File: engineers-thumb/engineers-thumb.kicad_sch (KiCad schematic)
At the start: 46 parts, among them J1 power, J2 Conn_01x06_Female, Q1 BC556, U1 LM13700, U2 TL074

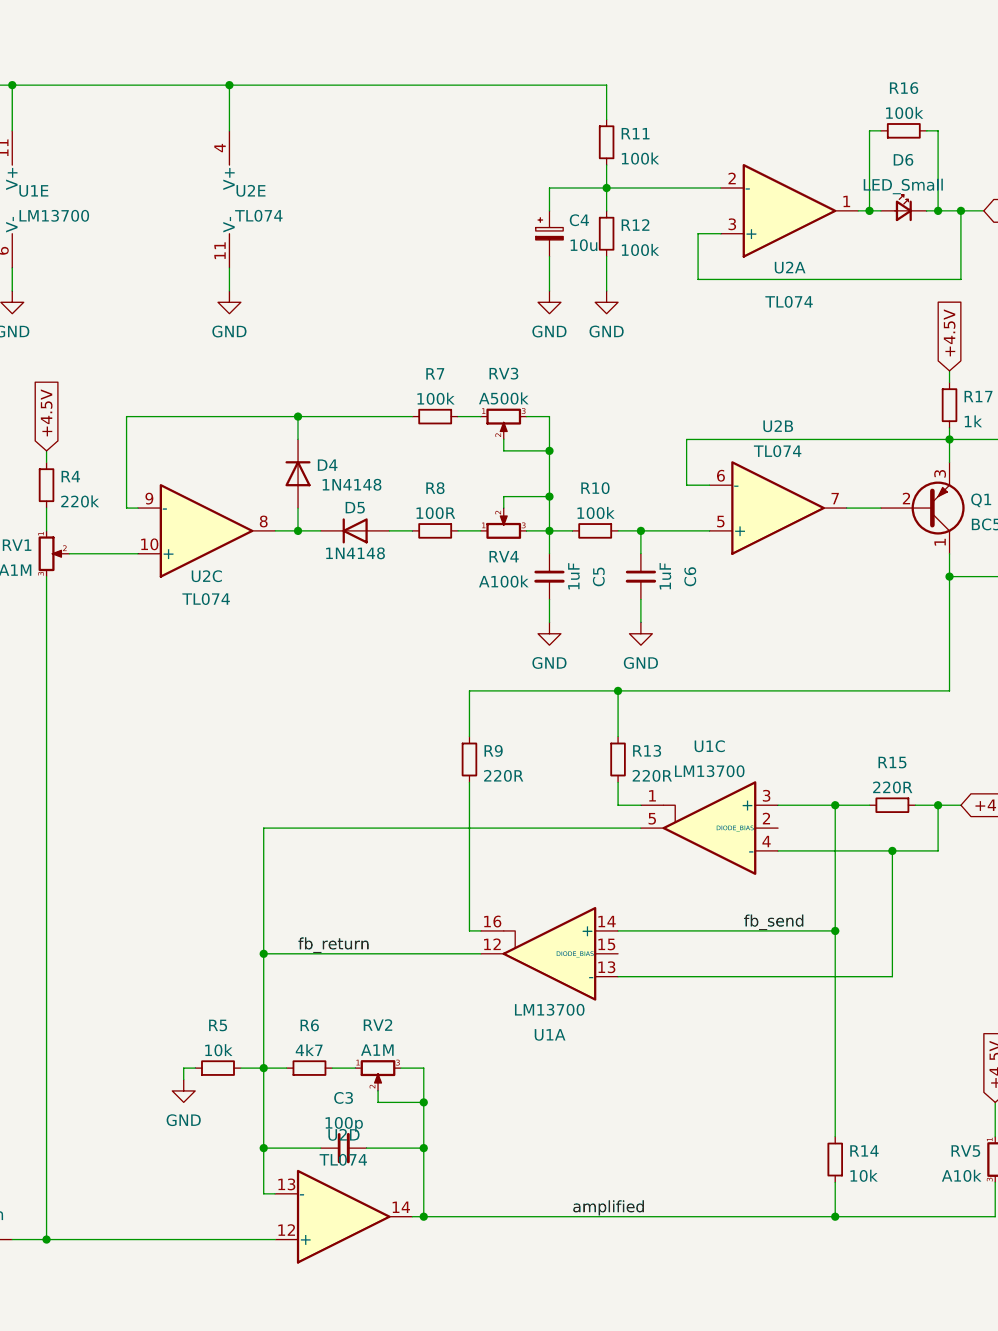
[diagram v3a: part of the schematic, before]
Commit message: Added compressor and psu schematics.
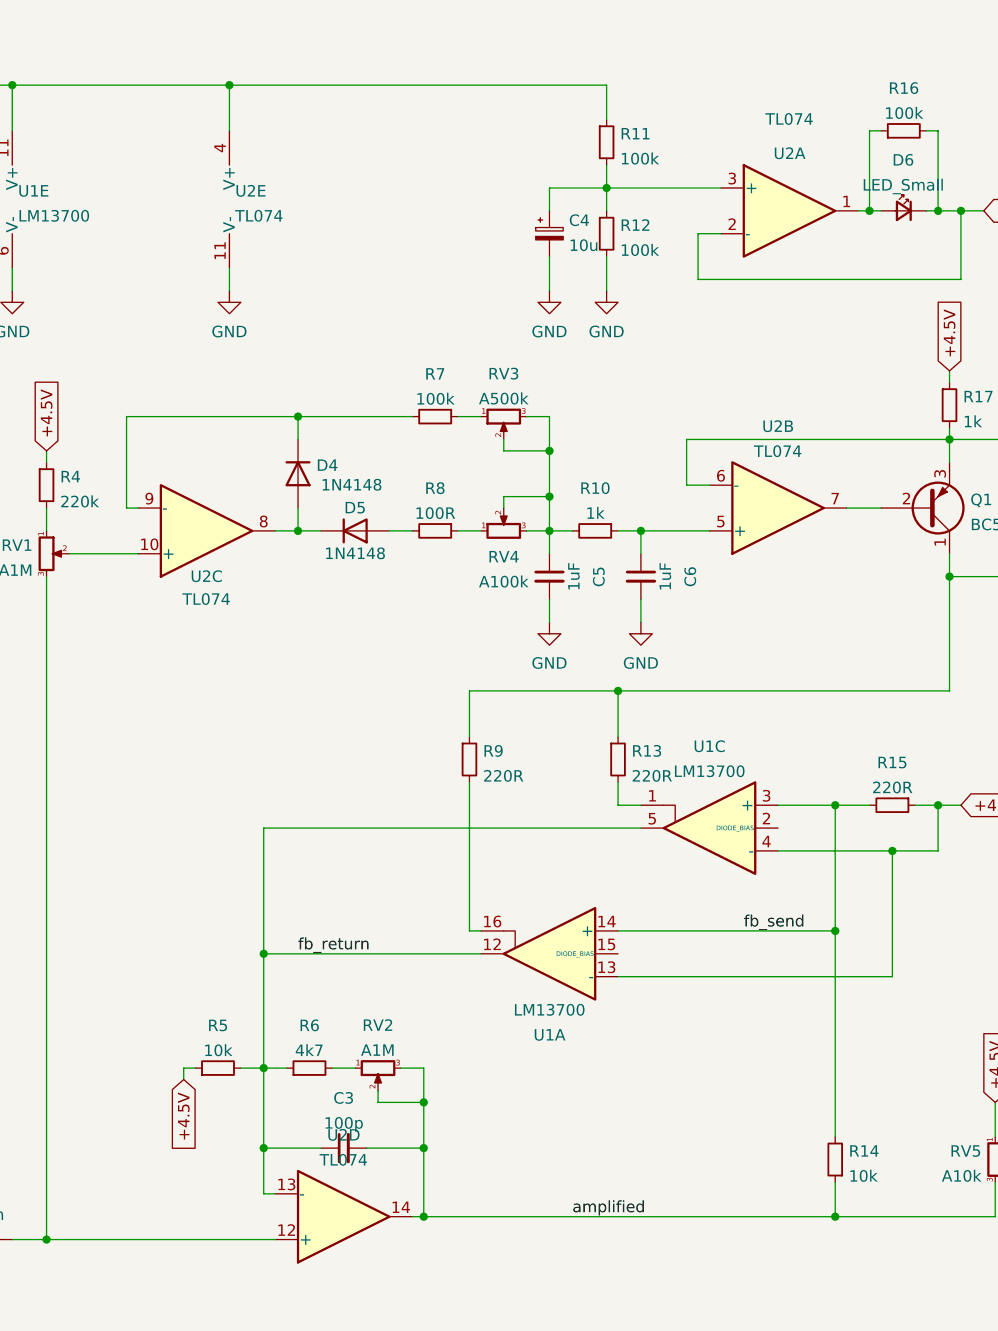
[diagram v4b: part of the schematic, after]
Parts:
- R10: value 100k -> 1k
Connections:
- net +4.5V: now also R5.1, U2.2 (-); no longer U2.3 (+)
- net GND: no longer R5.1
- net at C4.1, R11.2, R12.1: now also U2.3 (+); no longer U2.2 (-)
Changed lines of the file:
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@@
+    )
+  )
+  (global_label "+4.5V" (shape input) (at 88.9 130.81 270) (fields_autoplaced)
+    (effects (font (size 1.27 1.27)) (justify right))
+    (property "Intersheet References" "${INTERSHEET_REFS}" (id 0) (at 88.9794 138.9079 90)
+      (effects (font (size 1.27 1.27)) (justify right) hide)
     )
   )
@@
     (in_bom yes) (on_board yes) (fields_autoplaced)
     (property "Reference" "R10" (id 0) (at 134.62 65.1469 90))
-    (property "Value" "100k" (id 1) (at 134.62 67.922 90))
+    (property "Value" "1k" (id 1) (at 134.62 67.922 90))
     (property "Footprint" "PartsStash:R_Axial_DIN0207_L6.3mm_D2.5mm_P7.62mm_Horizontal" (id 2) (at 134.62 69.85 0)
       (effects (font (size 1.27 1.27)) hide)
@@
     (pin "11")
     (pin "6")
-  )
-  (symbol (lib_id "power:GND") (at 88.9 130.81 0) (unit 1)
-    (in_bom yes) (on_board yes) (fields_autoplaced)
-    (property "Reference" "#PWR08" (id 0) (at 88.9 137.16 0)
-      (effects (font (size 1.27 1.27)) hide)
-    )
-    (property "Value" "GND" (id 1) (at 88.9 135.3725 0))
-    (property "Footprint" "" (id 2) (at 88.9 130.81 0)
-      (effects (font (size 1.27 1.27)) hide)
-    )
-    (property "Datasheet" "" (id 3) (at 88.9 130.81 0)
-      (effects (font (size 1.27 1.27)) hide)
-    )
-    (pin "1")
   )
   (symbol (lib_id "power:GND") (at 218.44 151.13 0) (unit 1)
@@
     (pin "3")
   )
-  (symbol (lib_id "Amplifier_Operational:TL074") (at 156.21 34.29 0) (mirror x) (unit 1)
+  (symbol (lib_id "Amplifier_Operational:TL074") (at 156.21 34.29 0) (unit 1)
     (in_bom yes) (on_board yes)
-    (property "Reference" "U2" (id 0) (at 156.21 40.64 0))
-    (property "Value" "TL074" (id 1) (at 156.21 44.45 0))
-    (property "Footprint" "Package_DIP:DIP-14_W7.62mm_Socket_LongPads" (id 2) (at 154.94 36.83 0)
-      (effects (font (size 1.27 1.27)) hide)
-    )
-    (property "Datasheet" "http://www.ti.com/lit/ds/symlink/tl071.pdf" (id 3) (at 157.48 39.37 0)
+    (property "Reference" "U2" (id 0) (at 156.21 27.94 0))
+    (property "Value" "TL074" (id 1) (at 156.21 24.13 0))
+    (property "Footprint" "Package_DIP:DIP-14_W7.62mm_Socket_LongPads" (id 2) (at 154.94 31.75 0)
+      (effects (font (size 1.27 1.27)) hide)
+    )
+    (property "Datasheet" "http://www.ti.com/lit/ds/symlink/tl071.pdf" (id 3) (at 157.48 29.21 0)
       (effects (font (size 1.27 1.27)) hide)
     )
@@
       (reference "#PWR07") (unit 1) (value "GND") (footprint "")
     )
-    (path "/0c3a9905-caf7-40ca-a040-de0baeb38479"
-      (reference "#PWR08") (unit 1) (value "GND") (footprint "")
-    )
     (path "/5c27f58f-49a5-492a-9913-b8da62d963a5"
       (reference "#PWR09") (unit 1) (value "GND") (footprint "")
@@
     )
     (path "/02df730c-f0d5-46ee-ab40-7905f99f91de"
-      (reference "R10") (unit 1) (value "100k") (footprint "PartsStash:R_Axial_DIN0207_L6.3mm_D2.5mm_P7.62mm_Horizontal")
+      (reference "R10") (unit 1) (value "1k") (footprint "PartsStash:R_Axial_DIN0207_L6.3mm_D2.5mm_P7.62mm_Horizontal")
     )
     (path "/082ecb16-bdc7-404f-9607-610400050981"
